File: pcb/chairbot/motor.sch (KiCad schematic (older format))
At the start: 12 parts

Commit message: Work.
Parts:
- C5, C6, C7: renamed from C?; footprint (none) -> Capacitor_SMD:C_0603_1608Metric
- D2: renamed from D?; value D_Schottky -> SS34; footprint (none) -> Diode_SMD:D_SMC
- J3: renamed from J?; footprint (none) -> Connector_JST:JST_XH_B02B-XH-A_1x02_P2.50mm_Vertical
- Q1: renamed from Q?; footprint Package_TO_SOT_THT:TO-92_Inline -> Package_TO_SOT_SMD:SOT-223
- R1, R2: renamed from R?; footprint (none) -> Resistor_SMD:R_0603_1608Metric
- U2: renamed from U?; footprint (none) -> Package_SO:TSSOP-14_4.4x5mm_P0.65mm
- U6, U7: renamed from U?; footprint (none) -> Connector_PinSocket_2.54mm:PinSocket_2x04_P2.54mm_Horizontal
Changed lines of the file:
@@
 $EndDescr
 $Comp
-L chairbot:Motor_driver U?
+L chairbot:Motor_driver U7
 U 1 1 5BC5FCEE
 P 7450 3700
-F 0 "U?" H 7778 3746 50  0000 L CNN
+F 0 "U7" H 7778 3746 50  0000 L CNN
 F 1 "Motor_driver" H 7778 3655 50  0000 L CNN
-F 2 "" H 7350 3850 50  0001 C CNN
+F 2 "Connector_PinSocket_2.54mm:PinSocket_2x04_P2.54mm_Horizontal" H 7350 3850 50  0001 C CNN
 F 3 "" H 7350 3850 50  0001 C CNN
 	1    7450 3700
@@
 $EndComp
 $Comp
-L Transistor_FET:BS107 Q?
+L Transistor_FET:BS107 Q1
 U 1 1 5BC5FCF5
 P 6950 5400
-F 0 "Q?" H 7156 5446 50  0000 L CNN
+F 0 "Q1" H 7156 5446 50  0000 L CNN
 F 1 "ZXMN4A06G" H 7156 5355 50  0000 L CNN
-F 2 "Package_TO_SOT_THT:TO-92_Inline" H 7150 5325 50  0001 L CIN
+F 2 "Package_TO_SOT_SMD:SOT-223" H 7150 5325 50  0001 L CIN
 F 3 "http://www.onsemi.com/pub_link/Collateral/BS107-D.PDF" H 6950 5400 50  0001 L CNN
 	1    6950 5400
@@
 $EndComp
 $Comp
-L Connector_Generic:Conn_01x02 J?
+L Connector_Generic:Conn_01x02 J3
 U 1 1 5BC5FCFC
 P 7400 5000
-F 0 "J?" H 7480 4992 50  0000 L CNN
+F 0 "J3" H 7480 4992 50  0000 L CNN
 F 1 "Conn_01x02" H 7480 4901 50  0000 L CNN
-F 2 "" H 7400 5000 50  0001 C CNN
+F 2 "Connector_JST:JST_XH_B02B-XH-A_1x02_P2.50mm_Vertical" H 7400 5000 50  0001 C CNN
 F 3 "~" H 7400 5000 50  0001 C CNN
 	1    7400 5000
@@
 $EndComp
 $Comp
-L Device:R R?
+L Device:R R1
 U 1 1 5BC5FD15
 P 6550 5400
-F 0 "R?" V 6500 5250 50  0000 C CNN
+F 0 "R1" V 6500 5250 50  0000 C CNN
 F 1 "1K" V 6434 5400 50  0000 C CNN
-F 2 "" V 6480 5400 50  0001 C CNN
+F 2 "Resistor_SMD:R_0603_1608Metric" V 6480 5400 50  0001 C CNN
 F 3 "~" H 6550 5400 50  0001 C CNN
 	1    6550 5400
@@
 $EndComp
 $Comp
-L 74xx_IEEE:7408 U?
+L 74xx_IEEE:7408 U2
 U 1 1 5BC5FD1D
 P 5900 2250
-F 0 "U?" H 5900 2666 50  0000 C CNN
+F 0 "U2" H 5900 2666 50  0000 C CNN
 F 1 "74HCT08" H 5900 2575 50  0000 C CNN
-F 2 "" H 5900 2250 50  0001 C CNN
+F 2 "Package_SO:TSSOP-14_4.4x5mm_P0.65mm" H 5900 2250 50  0001 C CNN
 F 3 "" H 5900 2250 50  0001 C CNN
 	1    5900 2250
@@
 	6750 1850 6950 1850
 $Comp
-L 74xx_IEEE:7408 U?
+L 74xx_IEEE:7408 U2
 U 2 1 5BC5FD27
 P 5950 3650
-F 0 "U?" H 5950 4066 50  0000 C CNN
+F 0 "U2" H 5950 4066 50  0000 C CNN
 F 1 "74HCT08" H 5950 3975 50  0000 C CNN
-F 2 "" H 5950 3650 50  0001 C CNN
+F 2 "Package_SO:TSSOP-14_4.4x5mm_P0.65mm" H 5950 3650 50  0001 C CNN
 F 3 "" H 5950 3650 50  0001 C CNN
 	2    5950 3650
@@
 $EndComp
 $Comp
-L Device:C C?
+L Device:C C5
 U 1 1 5BC5FD46
 P 6150 1800
-F 0 "C?" V 5898 1800 50  0000 C CNN
+F 0 "C5" V 5898 1800 50  0000 C CNN
 F 1 "100n" V 5989 1800 50  0000 C CNN
-F 2 "" H 6188 1650 50  0001 C CNN
+F 2 "Capacitor_SMD:C_0603_1608Metric" H 6188 1650 50  0001 C CNN
 F 3 "~" H 6150 1800 50  0001 C CNN
 	1    6150 1800
@@
 	6400 1800 6400 1900
 $Comp
-L Device:C C?
+L Device:C C6
 U 1 1 5BC5FD59
 P 8000 1400
-F 0 "C?" H 8115 1446 50  0000 L CNN
+F 0 "C6" H 8115 1446 50  0000 L CNN
 F 1 "100n" H 8115 1355 50  0000 L CNN
-F 2 "" H 8038 1250 50  0001 C CNN
+F 2 "Capacitor_SMD:C_0603_1608Metric" H 8038 1250 50  0001 C CNN
 F 3 "~" H 8000 1400 50  0001 C CNN
 	1    8000 1400
@@
 $EndComp
 $Comp
-L Device:C C?
+L Device:C C7
 U 1 1 5BC5FD66
 P 8000 3200
-F 0 "C?" H 8115 3246 50  0000 L CNN
+F 0 "C7" H 8115 3246 50  0000 L CNN
 F 1 "100n" H 8115 3155 50  0000 L CNN
-F 2 "" H 8038 3050 50  0001 C CNN
+F 2 "Capacitor_SMD:C_0603_1608Metric" H 8038 3050 50  0001 C CNN
 F 3 "~" H 8000 3200 50  0001 C CNN
 	1    8000 3200
@@
 	7650 4350 7450 4350
 $Comp
-L Device:D_Schottky D?
+L Device:D_Schottky D2
 U 1 1 5BC5FD93
 P 6800 5100
-F 0 "D?" H 6800 5316 50  0000 C CNN
-F 1 "D_Schottky" H 6800 5225 50  0000 C CNN
-F 2 "" H 6800 5100 50  0001 C CNN
+F 0 "D2" H 6800 5316 50  0000 C CNN
+F 1 "SS34" H 6800 5225 50  0000 C CNN
+F 2 "Diode_SMD:D_SMC" H 6800 5100 50  0001 C CNN
 F 3 "~" H 6800 5100 50  0001 C CNN
 	1    6800 5100
@@
 Connection ~ 7050 5100
 $Comp
-L chairbot:Motor_driver U?
+L chairbot:Motor_driver U6
 U 1 1 5BC5FDA0
 P 7450 1900
-F 0 "U?" H 7778 1946 50  0000 L CNN
+F 0 "U6" H 7778 1946 50  0000 L CNN
 F 1 "Motor_driver" H 7778 1855 50  0000 L CNN
-F 2 "" H 7350 2050 50  0001 C CNN
+F 2 "Connector_PinSocket_2.54mm:PinSocket_2x04_P2.54mm_Horizontal" H 7350 2050 50  0001 C CNN
 F 3 "" H 7350 2050 50  0001 C CNN
 	1    7450 1900
@@
 	4750 3550 5400 3550
 $Comp
-L Device:R R?
+L Device:R R2
 U 1 1 5BD21085
 P 6550 5600
-F 0 "R?" V 6500 5450 50  0000 C CNN
+F 0 "R2" V 6500 5450 50  0000 C CNN
 F 1 "10K" V 6700 5600 50  0000 C CNN
-F 2 "" V 6480 5600 50  0001 C CNN
+F 2 "Resistor_SMD:R_0603_1608Metric" V 6480 5600 50  0001 C CNN
 F 3 "~" H 6550 5600 50  0001 C CNN
 	1    6550 5600

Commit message: Work work work.
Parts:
- removed unit 2 of U2
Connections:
- net labels added: EN
- net labels removed: EN_A, EN_B
- wire segments 67 -> 64
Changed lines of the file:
@@
 Wire Wire Line
 	6750 1850 6950 1850
-$Comp
-L 74xx_IEEE:7408 U2
-U 2 1 5BC5FD27
-P 5950 3650
-F 0 "U2" H 5950 4066 50  0000 C CNN
-F 1 "74HCT08" H 5950 3975 50  0000 C CNN
-F 2 "Package_SO:TSSOP-14_4.4x5mm_P0.65mm" H 5950 3650 50  0001 C CNN
-F 3 "" H 5950 3650 50  0001 C CNN
-	2    5950 3650
-	1    0    0    -1
-$EndComp
-Wire Wire Line
-	6500 3650 6750 3650
 Wire Wire Line
 	6750 3650 6750 3750
 Wire Wire Line
 	6750 3750 6950 3750
-Connection ~ 6750 3650
 Wire Wire Line
 	6750 3650 6950 3650
@@
 	6650 1400 4750 1400
 Wire Wire Line
-	6750 2950 6750 3350
-Wire Wire Line
-	6750 3350 6950 3350
-Wire Wire Line
-	6950 3450 6650 3450
-Wire Wire Line
-	6650 3450 6650 3100
+	6550 2950 6550 3350
+Wire Wire Line
+	6550 3350 6950 3350
+Wire Wire Line
+	6950 3450 6450 3450
+Wire Wire Line
+	6450 3450 6450 3100
 Text GLabel 4050 5400 0    50   Input ~ 0
 Brake
@@
 	4050 5400 5350 5400
 Wire Wire Line
-	5350 2350 5350 3750
-Wire Wire Line
-	5400 3750 5350 3750
-Connection ~ 5350 3750
-Wire Wire Line
-	5350 3750 5350 5400
-Wire Wire Line
 	5900 2500 5900 2650
-Text GLabel 6650 2500 0    50   Input ~ 0
+Text GLabel 6500 2500 0    50   Input ~ 0
 IS_A_L
-Text GLabel 6650 2700 0    50   Input ~ 0
+Text GLabel 6500 2700 0    50   Input ~ 0
 IS_A_R
 Wire Wire Line
 	6950 2250 6950 2700
 Wire Wire Line
-	6950 2700 6650 2700
+	6950 2700 6500 2700
 Wire Wire Line
 	6950 2150 6850 2150
@@
 	6850 2150 6850 2500
 Wire Wire Line
-	6850 2500 6650 2500
+	6850 2500 6500 2500
 Text GLabel 6650 3950 0    50   Input ~ 0
 IS_B_L
@@
 PWM_B_R
 Wire Wire Line
-	4750 2950 6750 2950
-Wire Wire Line
-	4750 3100 6650 3100
+	4750 2950 6550 2950
+Wire Wire Line
+	4750 3100 6450 3100
 Text GLabel 4750 2150 0    50   Input ~ 0
-EN_A
+EN
 Wire Wire Line
 	4750 2150 5350 2150
-Text GLabel 4750 3550 0    50   Input ~ 0
-EN_B
-Wire Wire Line
-	4750 3550 5400 3550
 $Comp
 L Device:R R2
@@
 Connection ~ 6300 5400
 Connection ~ 5350 5400
+Wire Wire Line
+	5350 2350 5350 5400
+Wire Wire Line
+	6750 2250 6750 3650
+Connection ~ 6750 2250
+Connection ~ 6750 3650
 $EndSCHEMATC

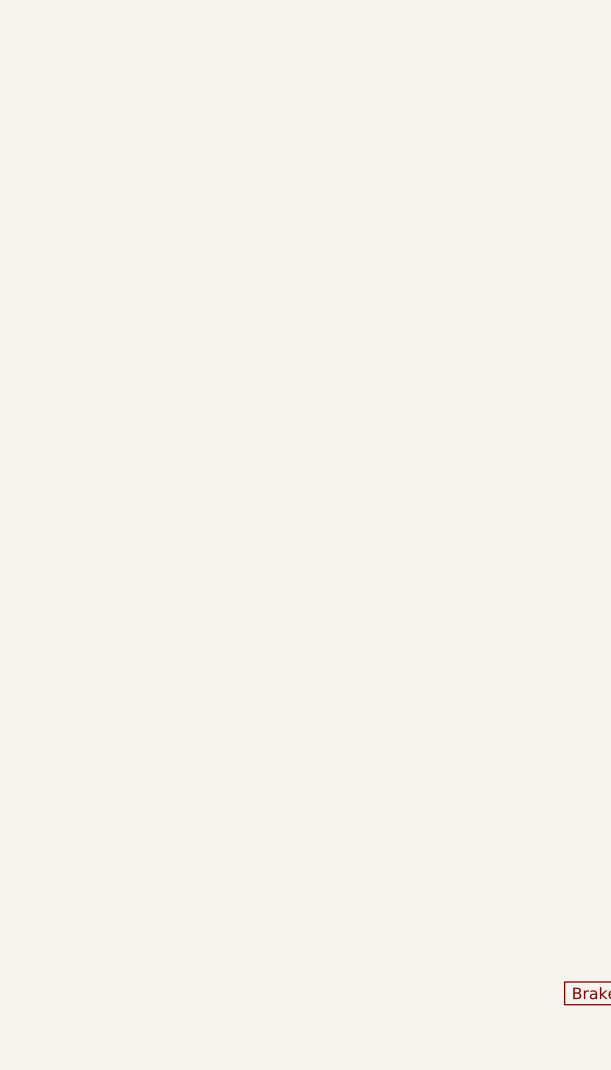
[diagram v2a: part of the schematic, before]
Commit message: Add proper footprint for peak detector.
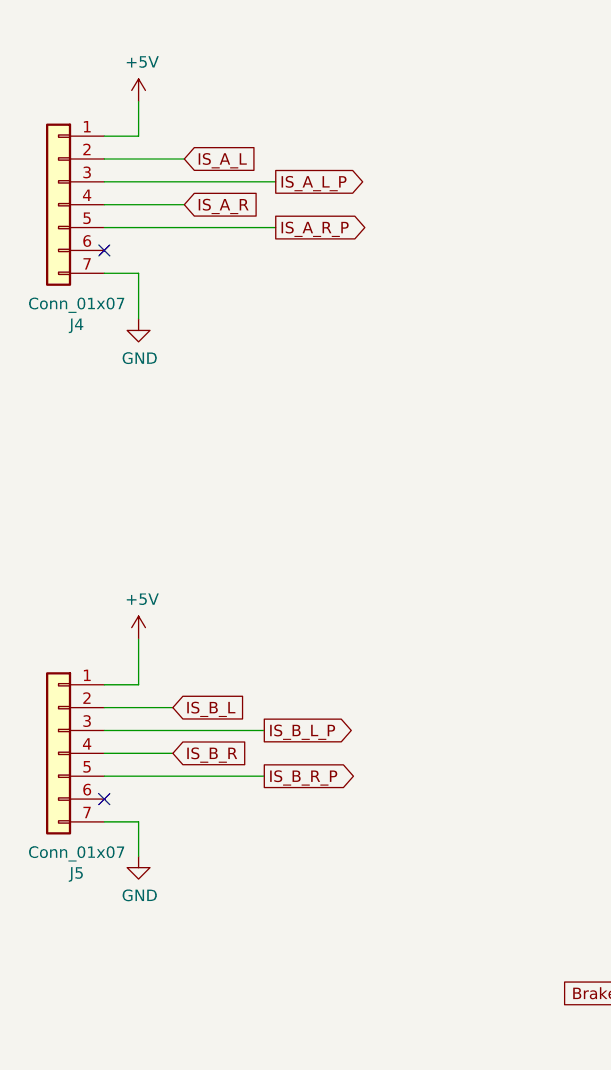
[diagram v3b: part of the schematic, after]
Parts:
- added J4, J5: Conn_01x07, chairbot:peakdetector, symbol Connector_Generic:Conn_01x07
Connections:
- net labels added: IS_A_L_P, IS_A_R_P, IS_B_L_P, IS_B_R_P
- wire segments 64 -> 80
- no-connect marks 0 -> 2
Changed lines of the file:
@@
 Connection ~ 6750 2250
 Connection ~ 6750 3650
+$Comp
+L Connector_Generic:Conn_01x07 J5
+U 1 1 5BDF1CC6
+P 1550 4350
+F 0 "J5" H 1470 3825 50  0000 C CNN
+F 1 "Conn_01x07" H 1470 3916 50  0000 C CNN
+F 2 "chairbot:peakdetector" H 1550 4350 50  0001 C CNN
+F 3 "~" H 1550 4350 50  0001 C CNN
+	1    1550 4350
+	-1   0    0    -1
+$EndComp
+$Comp
+L Connector_Generic:Conn_01x07 J4
+U 1 1 5BDF1D76
+P 1550 1950
+F 0 "J4" H 1470 1425 50  0000 C CNN
+F 1 "Conn_01x07" H 1470 1516 50  0000 C CNN
+F 2 "chairbot:peakdetector" H 1550 1950 50  0001 C CNN
+F 3 "~" H 1550 1950 50  0001 C CNN
+	1    1550 1950
+	-1   0    0    -1
+$EndComp
+$Comp
+L power:+5V #PWR0126
+U 1 1 5BDFA834
+P 1900 1500
+F 0 "#PWR0126" H 1900 1350 50  0001 C CNN
+F 1 "+5V" H 1915 1673 50  0000 C CNN
+F 2 "" H 1900 1500 50  0001 C CNN
+F 3 "" H 1900 1500 50  0001 C CNN
+	1    1900 1500
+	1    0    0    -1
+$EndComp
+Wire Wire Line
+	1900 1500 1900 1650
+Wire Wire Line
+	1900 1650 1750 1650
+$Comp
+L power:GND #PWR0127
+U 1 1 5BDFBE65
+P 1900 2450
+F 0 "#PWR0127" H 1900 2200 50  0001 C CNN
+F 1 "GND" H 1905 2277 50  0000 C CNN
+F 2 "" H 1900 2450 50  0001 C CNN
+F 3 "" H 1900 2450 50  0001 C CNN
+	1    1900 2450
+	1    0    0    -1
+$EndComp
+Wire Wire Line
+	1750 2250 1900 2250
+Wire Wire Line
+	1900 2250 1900 2450
+$Comp
+L power:GND #PWR0128
+U 1 1 5BDFD5FF
+P 1900 4800
+F 0 "#PWR0128" H 1900 4550 50  0001 C CNN
+F 1 "GND" H 1905 4627 50  0000 C CNN
+F 2 "" H 1900 4800 50  0001 C CNN
+F 3 "" H 1900 4800 50  0001 C CNN
+	1    1900 4800
+	1    0    0    -1
+$EndComp
+Wire Wire Line
+	1900 4800 1900 4650
+Wire Wire Line
+	1900 4650 1750 4650
+$Comp
+L power:+5V #PWR0129
+U 1 1 5BDFEF77
+P 1900 3850
+F 0 "#PWR0129" H 1900 3700 50  0001 C CNN
+F 1 "+5V" H 1915 4023 50  0000 C CNN
+F 2 "" H 1900 3850 50  0001 C CNN
+F 3 "" H 1900 3850 50  0001 C CNN
+	1    1900 3850
+	1    0    0    -1
+$EndComp
+Wire Wire Line
+	1900 3850 1900 4050
+Wire Wire Line
+	1900 4050 1750 4050
+NoConn ~ 1750 4550
+NoConn ~ 1750 2150
+Text GLabel 2100 1750 2    50   Input ~ 0
+IS_A_L
+Text GLabel 2100 1950 2    50   Input ~ 0
+IS_A_R
+Wire Wire Line
+	2100 1750 1750 1750
+Wire Wire Line
+	1750 1950 2100 1950
+Text GLabel 2050 4150 2    50   Input ~ 0
+IS_B_L
+Text GLabel 2050 4350 2    50   Input ~ 0
+IS_B_R
+Wire Wire Line
+	2050 4350 1750 4350
+Wire Wire Line
+	1750 4150 2050 4150
+Text GLabel 2450 4250 2    50   Output ~ 0
+IS_B_L_P
+Text GLabel 2450 4450 2    50   Output ~ 0
+IS_B_R_P
+Wire Wire Line
+	2450 4450 1750 4450
+Wire Wire Line
+	1750 4250 2450 4250
+Text GLabel 2500 1850 2    50   Output ~ 0
+IS_A_L_P
+Text GLabel 2500 2050 2    50   Output ~ 0
+IS_A_R_P
+Wire Wire Line
+	2500 2050 1750 2050
+Wire Wire Line
+	1750 1850 2500 1850
 $EndSCHEMATC

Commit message: Fix footprint for diodes.
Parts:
- D2: footprint Diode_SMD:D_SMC -> Diode_SMD:D_SMB
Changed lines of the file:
@@
 F 0 "D2" H 6800 5316 50  0000 C CNN
 F 1 "SS34" H 6800 5225 50  0000 C CNN
-F 2 "Diode_SMD:D_SMC" H 6800 5100 50  0001 C CNN
+F 2 "Diode_SMD:D_SMB" H 6800 5100 50  0001 C CNN
 F 3 "~" H 6800 5100 50  0001 C CNN
 	1    6800 5100

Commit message: Fix more stuff.
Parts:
- Q1: symbol Transistor_FET:BS107 -> Transistor_FET:BSP129
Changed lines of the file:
@@
 $EndComp
 $Comp
-L Transistor_FET:BS107 Q1
+L Transistor_FET:BSP129 Q1
 U 1 1 5BC5FCF5
 P 6950 5400

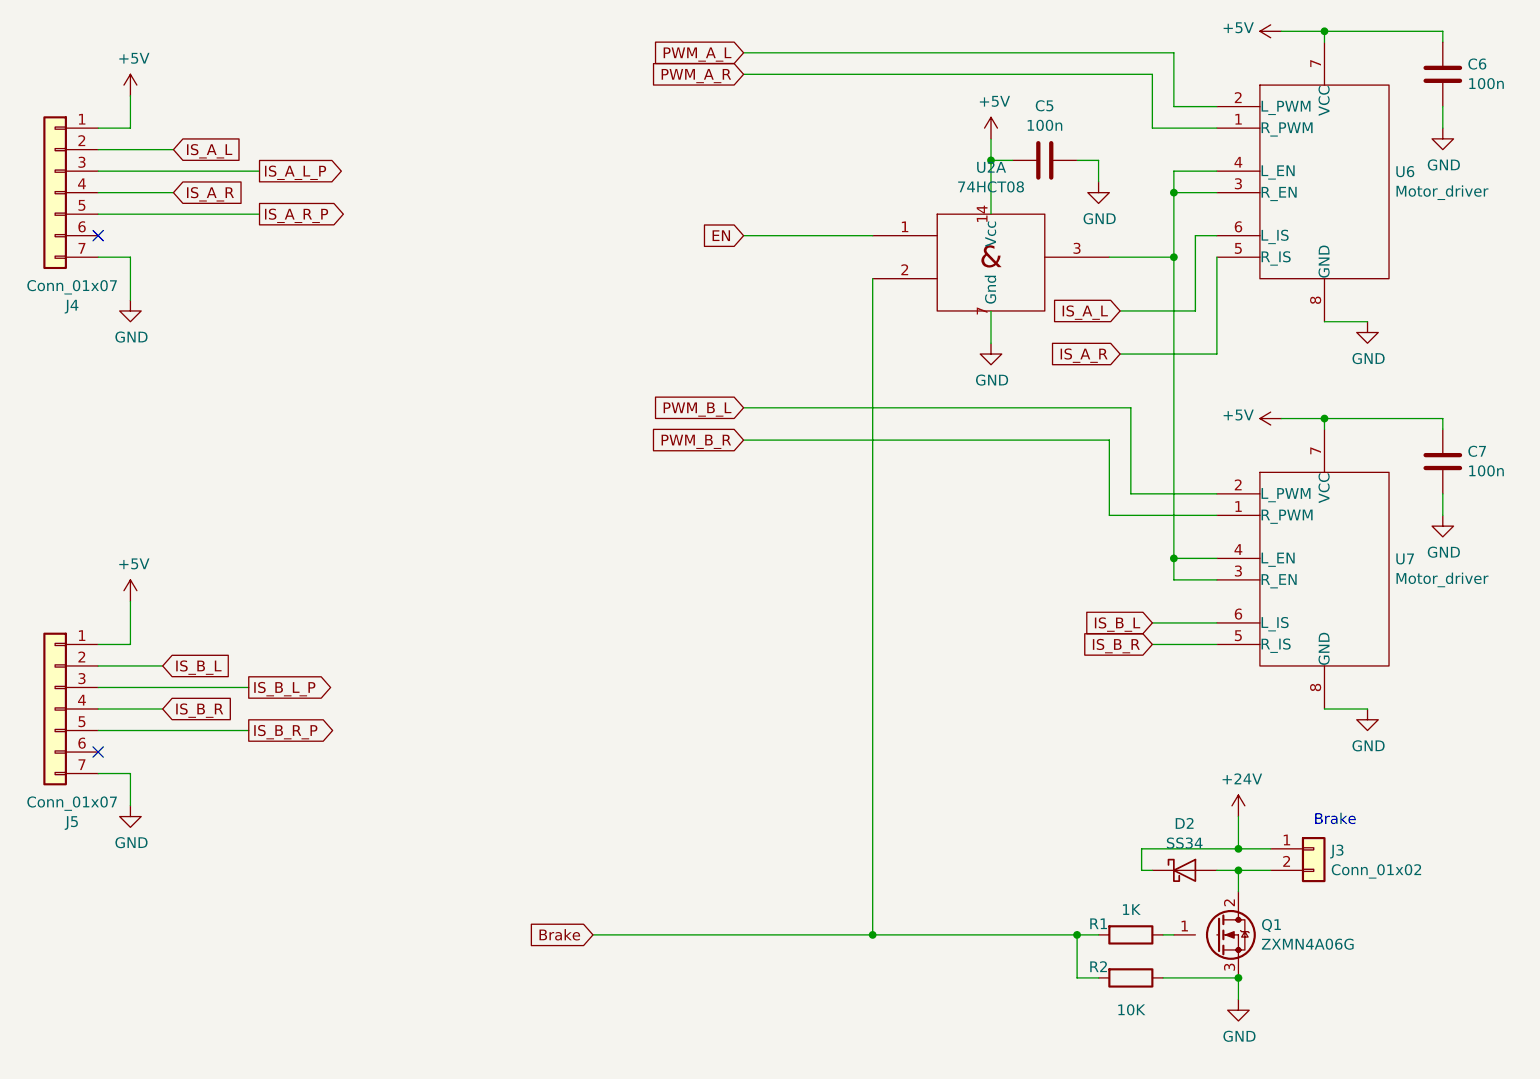
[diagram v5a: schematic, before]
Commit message: Tweak pin numbers.
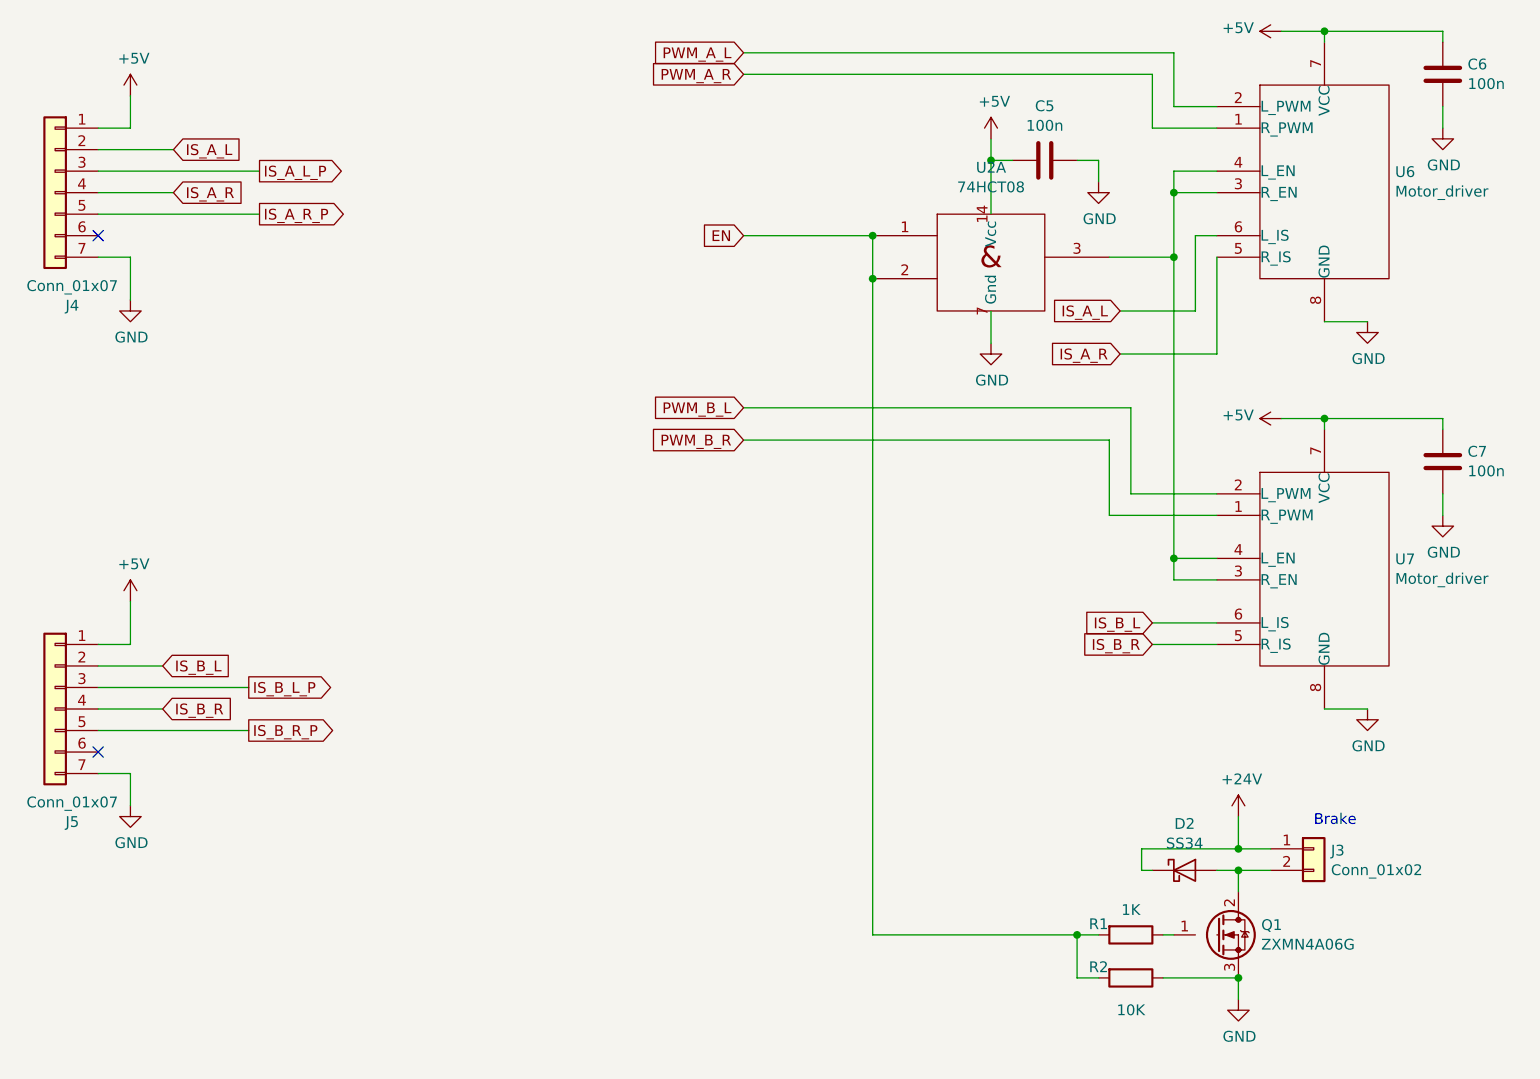
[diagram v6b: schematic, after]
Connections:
- net Brake is gone; now on net EN: R1.2, R2.2, U2.2
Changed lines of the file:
@@
 EESchema Schematic File Version 4
 LIBS:chairbot-cache
-EELAYER 26 0
+EELAYER 29 0
 EELAYER END
 $Descr A4 11693 8268
@@
 Wire Wire Line
 	6450 3450 6450 3100
-Text GLabel 4050 5400 0    50   Input ~ 0
-Brake
-Wire Wire Line
-	4050 5400 5350 5400
 Wire Wire Line
 	5900 2500 5900 2650
@@
 	6300 5400 5350 5400
 Connection ~ 6300 5400
-Connection ~ 5350 5400
 Wire Wire Line
 	5350 2350 5350 5400
@@
 Wire Wire Line
 	1750 1850 2500 1850
+Wire Wire Line
+	5350 2150 5350 2350
+Connection ~ 5350 2150
+Connection ~ 5350 2350
 $EndSCHEMATC
